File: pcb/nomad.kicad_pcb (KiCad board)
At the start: 2 copper layers, 60 x 100 mm, 42 parts, among them J1 USB_C_Receptacle_USB2.0_16P, J2 Conn_01x08_Pin, J4 Conn_Coaxial, SW1 UP, SW2 DOWN, SW3 RIGHT, SW4 LEFT, SW5 SEL, SW6 SW_Push, SW7 SW_Push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

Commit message: Adding silkscreen icons
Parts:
- removed the G*** at (154.1, 92.7)
- added C5: 10uF, Capacitor_SMD:C_0805_2012Metric, F.Cu at (116.6, 124.1)
- added C6: C, Capacitor_SMD:C_0805_2012Metric, F.Cu at (134.3, 117.7)
- added C7: C, Capacitor_SMD:C_0805_2012Metric, F.Cu at (133.0, 115.5)
- added C8: C, Capacitor_SMD:C_0805_2012Metric, F.Cu at (122.3, 120.1)
- added G***: LOGO, LOGO, F.Cu at (107.6, 53.7)
- added G***: LOGO, LOGO, F.Cu at (134.5, 135.0)
- added G***: LOGO, LOGO, F.Cu at (145.9, 47.6)
- added G***: LOGO, LOGO, F.Cu at (118.4, 93.0)
- added J3: Conn_Coaxial, Connector_Coaxial:U.FL_Hirose_U.FL-R-SMT-1_Vertical, F.Cu at (139.6, 47.0)
- added L2: 27nH, Inductor_SMD:L_0805_2012Metric, F.Cu at (135.4, 50.2)
- moved R8 12.1 mm to (148.1, 116.9)
- moved R16 6.10 mm to (155.7, 66.5), turned to 90 degrees
- moved U6 4.41 mm to (145.0, 57.5), turned to -90 degrees
- moved G*** 2.52 mm to (127.1, 58.7)
- moved U7 1.76 mm to (111.7, 122.8)
- moved C9 1.53 mm to (158.1, 61.3)
- moved C4 0.73 mm to (118.8, 124.1)
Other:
- board text removed: "LoRa"

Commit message: Updating schematic & pcb & BOM
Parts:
- added G***: LOGO, LOGO, F.Cu at (114.1, 138.8)
- moved J2 3.08 mm to (109.4, 74.4)
- moved G*** 2.70 mm to (121.1, 92.9)
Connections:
- U1 pad 36: unconnected-(U1-RXD0-Pad36) -> UART_TX
- U1 pad 37: unconnected-(U1-TXD0-Pad37) -> UART_RX
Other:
- board text added: "@OZane"
- board text added: "BOOT"
- board text added: "HackClub Fallout 2026"
- board text added: "In extreme situations remember to save your battery !"
- board text added: "RESET"

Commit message: Updating PCB
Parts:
- added G***: LOGO, LOGO, F.Cu at (128.9, 52.8)
- moved G*** 7.61 mm to (119.5, 58.4)
- moved G*** 2.62 mm to (164.1, 179.0)

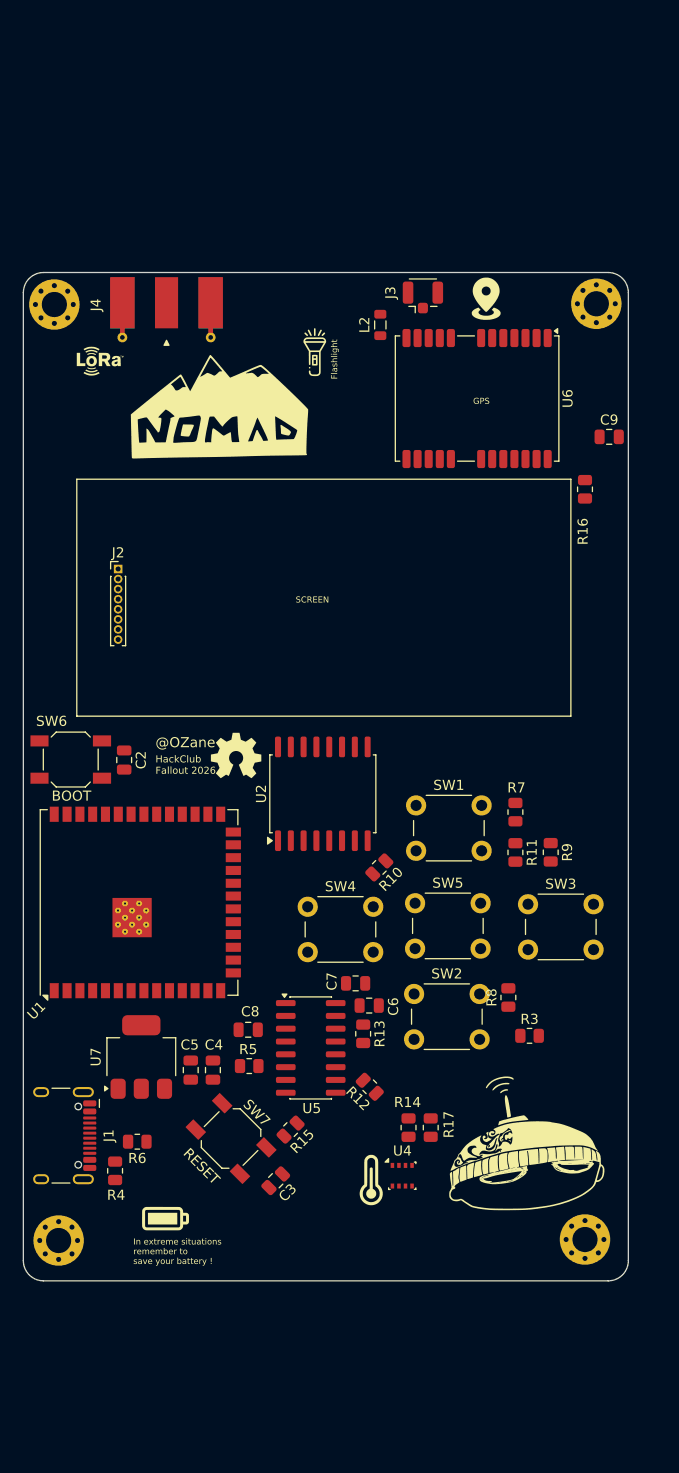
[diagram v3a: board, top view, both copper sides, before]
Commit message: Updating footprints & shematics + replacing components on PCB
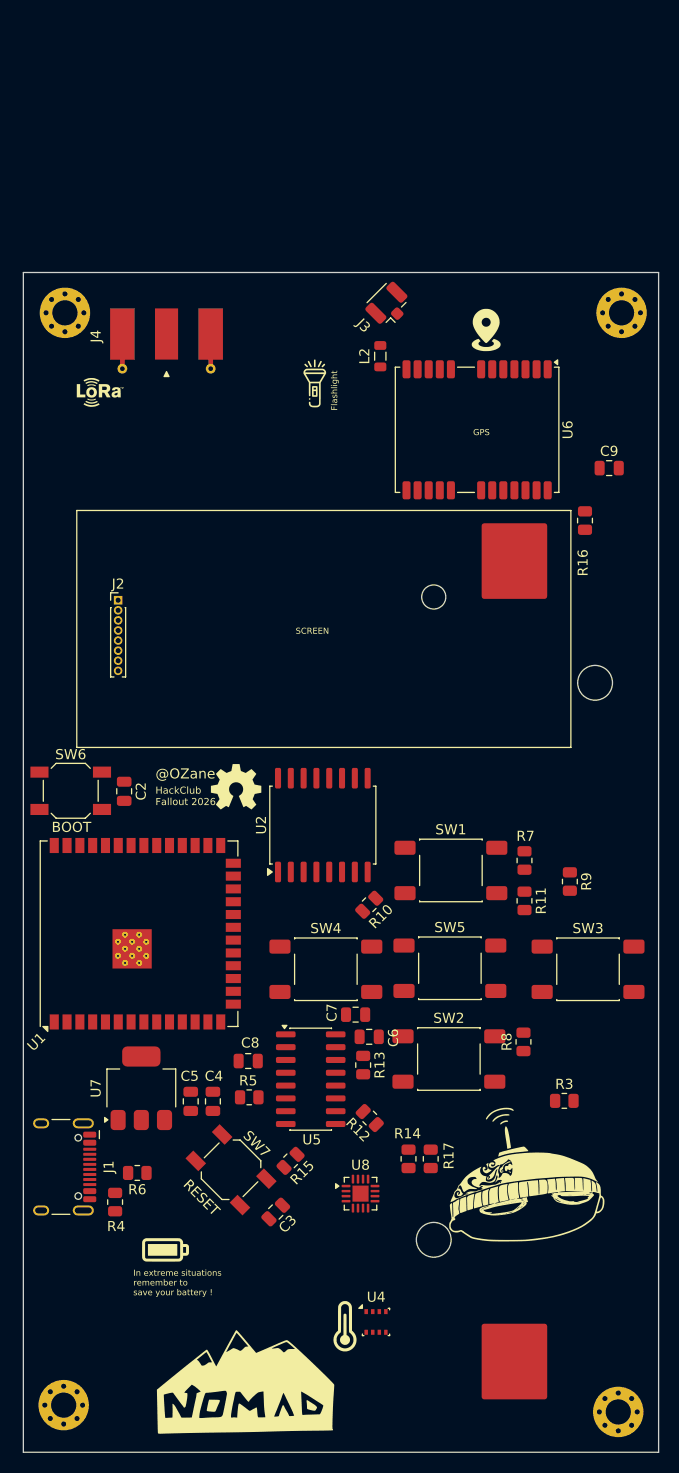
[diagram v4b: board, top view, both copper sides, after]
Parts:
- added REF**: BatteryHolder_Keystone_1042_1x18650, Battery:BatteryHolder_Keystone_1042_1x18650, B.Cu at (148.7, 113.3)
- added U8: BQ24075RGT, Package_DFN_QFN:VQFN-16-1EP_3x3mm_P0.5mm_EP1.6x1.6mm, F.Cu at (133.4, 136.3)
- SW1, SW2, SW3, SW4, SW5: footprint Button_Switch_THT:SW_PUSH_6mm -> Button_Switch_SMD:SW_Push_1P1T_NO_E-Switch_TL3301NxxxxxG
- moved G*** 96.7 mm to (122.1, 155.1)
- moved REF** 17.4 mm to (159.0, 158.0)
- moved REF** 16.3 mm to (104.0, 157.3)
- moved G*** 14.7 mm to (131.9, 149.5)
- moved U4 14.7 mm to (135.0, 149.1)
- moved SW3 8.78 mm to (156.0, 114.1)
- moved R3 7.31 mm to (153.7, 127.2)
- moved SW1 7.31 mm to (142.4, 104.3)
- moved SW5 7.31 mm to (142.3, 114.0)
- moved SW2 7.31 mm to (142.2, 123.0)
- moved SW4 6.46 mm to (130.0, 114.1)
- moved R11 4.88 mm to (149.7, 107.3)
- moved R7 4.88 mm to (149.7, 103.3)
- moved R8 4.65 mm to (149.6, 121.3)
- moved R10 3.83 mm to (134.3, 107.7)
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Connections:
- J2 pad 1: unconnected-(J2-Pin_1-Pad1) -> BLK
- J2 pad 2: unconnected-(J2-Pin_2-Pad2) -> CS
- J2 pad 3: unconnected-(J2-Pin_3-Pad3) -> DC
- J2 pad 4: unconnected-(J2-Pin_4-Pad4) -> RES
- J2 pad 5: unconnected-(J2-Pin_5-Pad5) -> SDA
- J2 pad 6: unconnected-(J2-Pin_6-Pad6) -> SCL
- J2 pad 7: unconnected-(J2-Pin_7-Pad7) -> +3V3
- J2 pad 8: unconnected-(J2-Pin_8-Pad8) -> GND
- J4 pad 2: unconnected-(J4-Ext-Pad2) -> GND
- U1 pad 12: unconnected-(U1-IO8-Pad12) -> SDA
- U1 pad 17: unconnected-(U1-IO9-Pad17) -> SCL
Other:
- board size 60 x 100 mm -> 63 x 117 mm

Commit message: Updating PCB
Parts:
- removed the REF** at (148.7, 113.3)
- removed U5: CH343G, Package_SO:SOIC-16_3.9x9.9mm_P1.27mm
- added ?: , , F.Cu at (114.4, 98.4)
- added ?: , , F.Cu at (114.6, 99.8)
- added C8: 100nF, Capacitor_SMD:C_0805_2012Metric, F.Cu at (126.4, 126.9)
- added REF**: JST_PH_S2B-PH-K_1x02_P2.00mm_Horizontal, Connector_JST:JST_PH_S2B-PH-K_1x02_P2.00mm_Horizontal, B.Cu at (149.8, 159.6)
- C7: value C -> 10nF
- moved G*** 10.6 mm to (159.6, 191.7)
- moved J4 3.03 mm to (114.2, 49.8)
- moved U8 1.23 mm to (133.2, 137.6)
- moved R14 1.00 mm to (139.2, 132.9)
- moved R17 1.00 mm to (141.4, 132.9)
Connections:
- C7 pad 2: +3V3 -> +5V
- U1 pad 13: unconnected-(U1-USB_D--Pad13) -> USB_D-
- U1 pad 14: unconnected-(U1-USB_D+-Pad14) -> USB_D+
- U1 pad 37: UART_RX -> unconnected-(U1-TXD0-Pad37)
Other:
- board text added: "Lora Module"

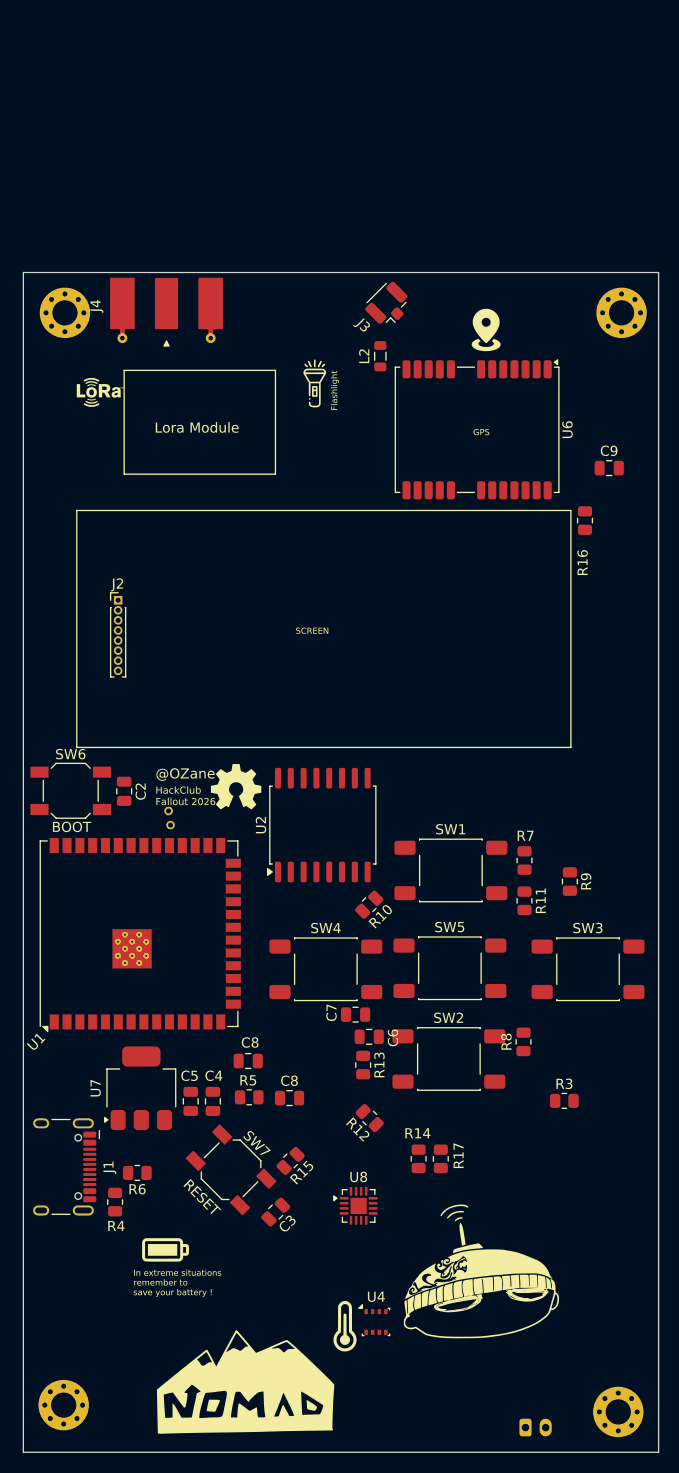
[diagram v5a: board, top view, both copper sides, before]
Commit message: Adding battery management system with  MCP73831 chip.
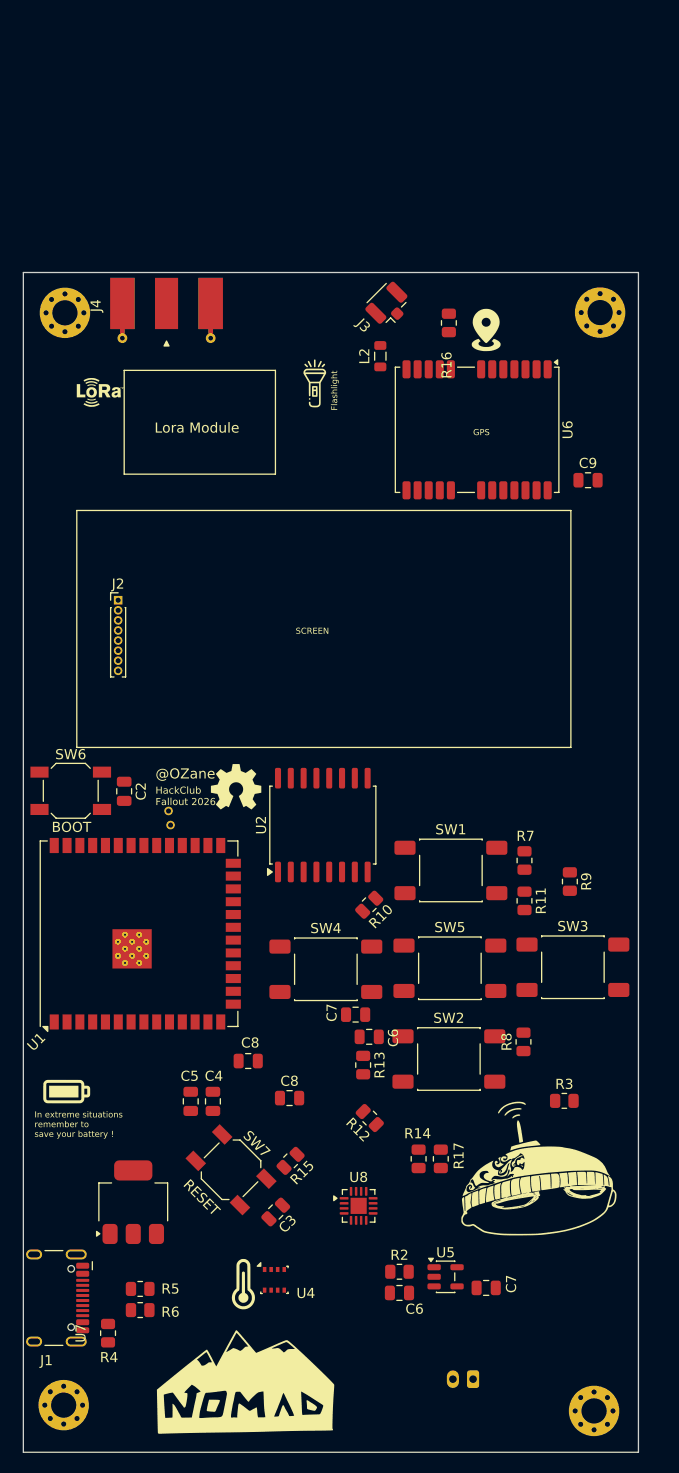
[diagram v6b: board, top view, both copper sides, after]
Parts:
- removed the REF** at (149.8, 159.6)
- added C6: C, Capacitor_SMD:C_0805_2012Metric, F.Cu at (137.3, 146.2)
- added C7: 4.7µF, Capacitor_SMD:C_0805_2012Metric, F.Cu at (145.9, 145.7)
- added J5: Conn_01x02_Pin, Connector_JST:JST_PH_S2B-PH-K_1x02_P2.00mm_Horizontal, B.Cu at (144.6, 154.8)
- added R2: 2K, Resistor_SMD:R_0805_2012Metric, F.Cu at (137.3, 144.1)
- added U5: MCP73831-2-OT, Package_TO_SOT_SMD:SOT-23-5, F.Cu at (141.9, 144.6)
- moved R16 23.8 mm to (142.2, 50.0)
- moved R5 21.9 mm to (111.6, 145.8)
- moved G*** 18.5 mm to (104.3, 126.2)
- moved R6 13.6 mm to (111.6, 147.9)
- moved J1 13.0 mm to (102.1, 146.7)
- moved R4 13.0 mm to (108.4, 150.2)
- moved G*** 11.7 mm to (165.3, 181.5)
- moved U7 11.3 mm to (110.9, 137.2)
- moved G*** 10.9 mm to (121.8, 145.3)
- moved U4 10.9 mm to (124.9, 144.9)
- moved C9 2.42 mm to (156.0, 65.6)
- moved REF** 2.40 mm to (156.6, 157.9)
- moved REF** 2.13 mm to (157.2, 49.0)
- moved SW3 1.51 mm to (154.5, 113.9)
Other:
- board size 63 x 117 mm -> 61 x 117 mm

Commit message: Updating footprints, PCb and schematics.
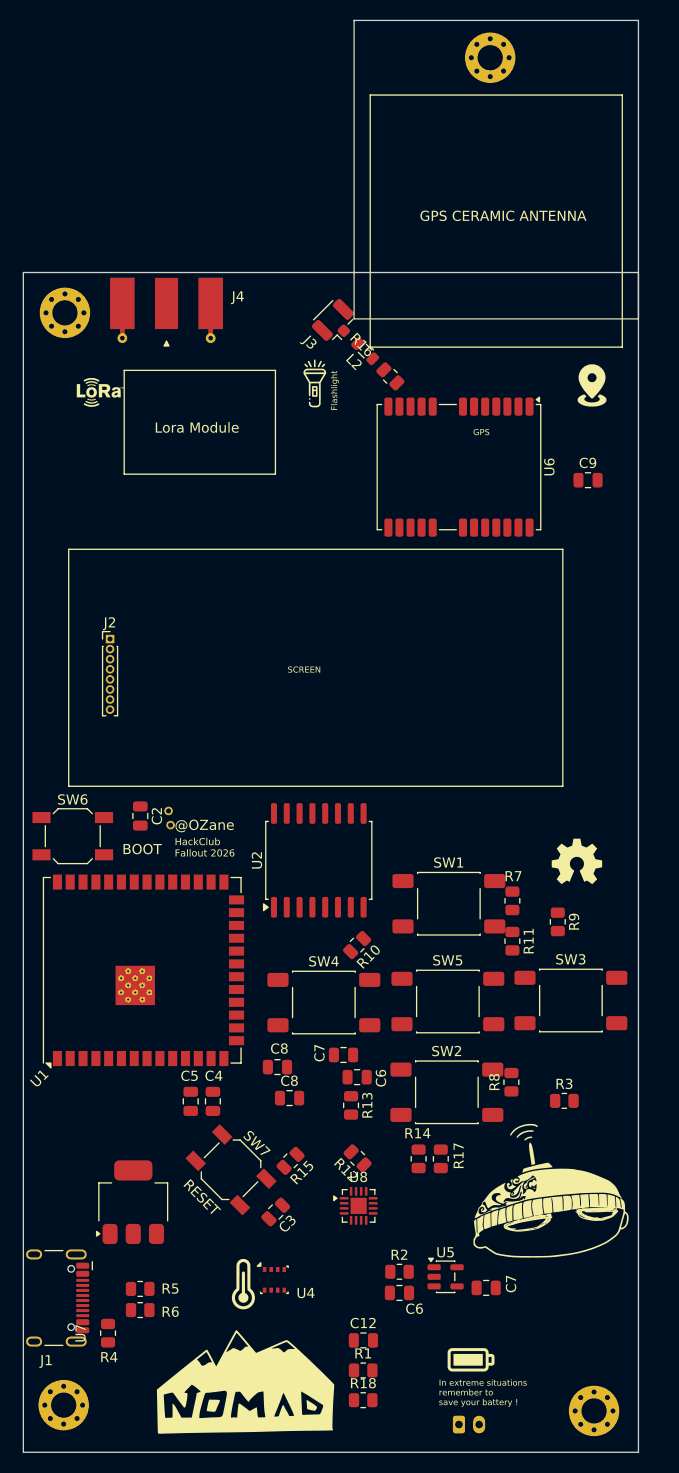
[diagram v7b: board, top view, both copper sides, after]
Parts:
- added C12: 0.1uF, Capacitor_SMD:C_0805_2012Metric, F.Cu at (133.7, 150.9)
- added R1: R, Resistor_SMD:R_0805_2012Metric, F.Cu at (133.7, 153.9)
- added R18: 470R, Resistor_SMD:R_0805_2012Metric, F.Cu at (133.7, 156.8)
- moved G*** 48.1 mm to (144.4, 152.8)
- moved G*** 34.6 mm to (154.9, 103.4)
- moved REF** 27.5 mm to (146.3, 23.7)
- moved G*** 11.9 mm to (156.4, 56.2)
- moved R16 7.86 mm to (136.4, 55.3), turned to -45 degrees
- moved J3 5.57 mm to (130.7, 49.7)
- moved J5 4.71 mm to (143.2, 159.2), turned to 0 degrees
- moved SW6 4.50 mm to (104.9, 100.9)
- moved C6 4.18 mm to (133.1, 124.8)
- moved R10 4.18 mm to (133.1, 111.7)
- moved C7 4.18 mm to (131.8, 122.6)
- moved R11 4.18 mm to (148.5, 111.3)
- moved R12 4.18 mm to (133.2, 132.9)
- moved R13 4.18 mm to (132.5, 127.6)
- moved R7 4.18 mm to (148.5, 107.3)
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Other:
- board size 61 x 117 mm -> 61 x 142 mm
- board text added: "GPS CERAMIC ANTENNA"

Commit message: Updating PCB
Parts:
- added Q2: 2N7002, Package_TO_SOT_SMD:SOT-23, F.Cu at (124.2, 50.8)
- R1: value R -> 1.5k
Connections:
- R1 pad 1: Net-(Q1-C) -> GND
- R1 pad 2: +3V3 -> Net-(Q2-S)
